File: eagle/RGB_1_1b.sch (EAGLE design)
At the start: 16 parts, among them X1 RGB, X2 Buzzer

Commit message: Missing doc files added, schematics.pdf created +doc/pdf/schematics.pdf: all schematics in one file
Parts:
- R2: value 4k7 -> 680
- R3: value 10k -> 4k7
- R4: value 2k2 -> 470
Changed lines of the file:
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@@
 <?xml version="1.0" encoding="utf-8"?>
 <!DOCTYPE eagle SYSTEM "eagle.dtd">
-<eagle version="7.6.0">
+<eagle version="8.3.2">
 <drawing>
 <settings>
 <setting alwaysvectorfont="no"/>
+<setting keepoldvectorfont="yes"/>
 <setting verticaltext="up"/>
 </settings>
@@
 <part name="P1" library="01-my-led" deviceset="RGB-5MM" device=""/>
 <part name="R1" library="01-my_rcl" deviceset="R-EU_" device="0207/10" value="220"/>
-<part name="R2" library="01-my_rcl" deviceset="R-EU_" device="0207/10" value="4k7"/>
-<part name="R3" library="01-my_rcl" deviceset="R-EU_" device="0207/10" value="10k"/>
-<part name="R4" library="01-my_rcl" deviceset="R-EU_" device="0207/10" value="2k2"/>
+<part name="R2" library="01-my_rcl" deviceset="R-EU_" device="0207/10" value="680"/>
+<part name="R3" library="01-my_rcl" deviceset="R-EU_" device="0207/10" value="4k7"/>
+<part name="R4" library="01-my_rcl" deviceset="R-EU_" device="0207/10" value="470"/>
 <part name="GND5" library="supply1" deviceset="GND" device=""/>
 <part name="P2" library="01-my-led" deviceset="LED" device="5MM"/>

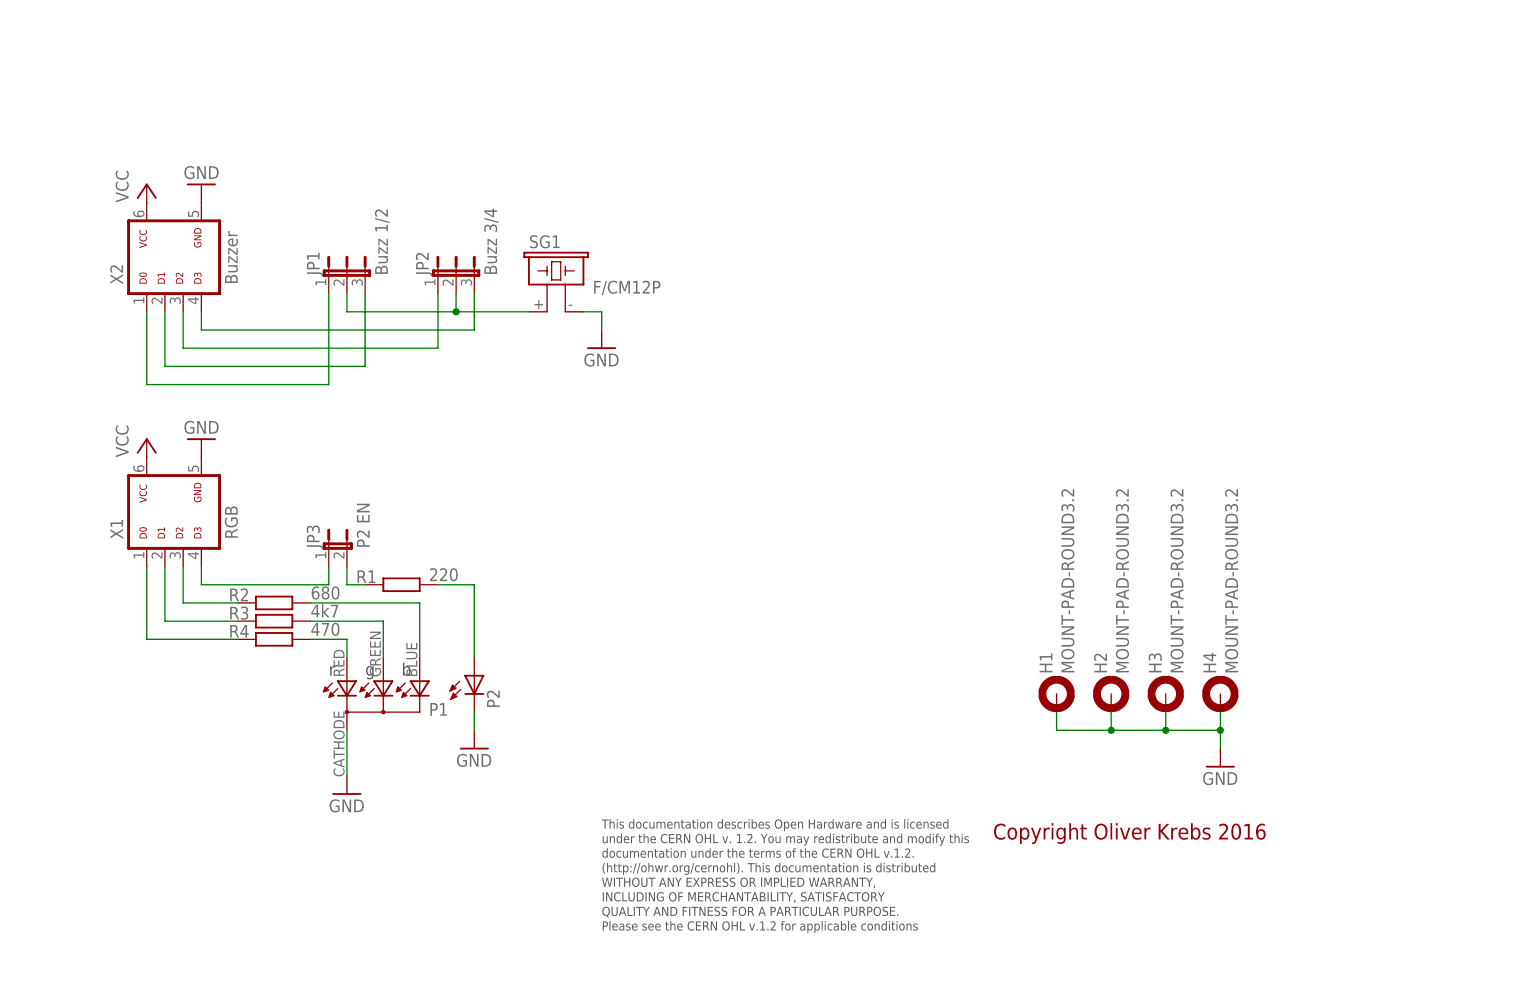
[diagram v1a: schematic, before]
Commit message: Add new tetra-Board and arduino files
Add AMP_1_0, AVC_1_0, D18_1_1, IOP_1_2, MIC_1_0, PIN_1_1, POT_1_0, PWA_1_0, PWR_1_0, RGF 2.0, SOC_2_0, VLT_1_0
Add mex_nano_shield_keyboard, mex_nano_shied_numbers

New arduino projects
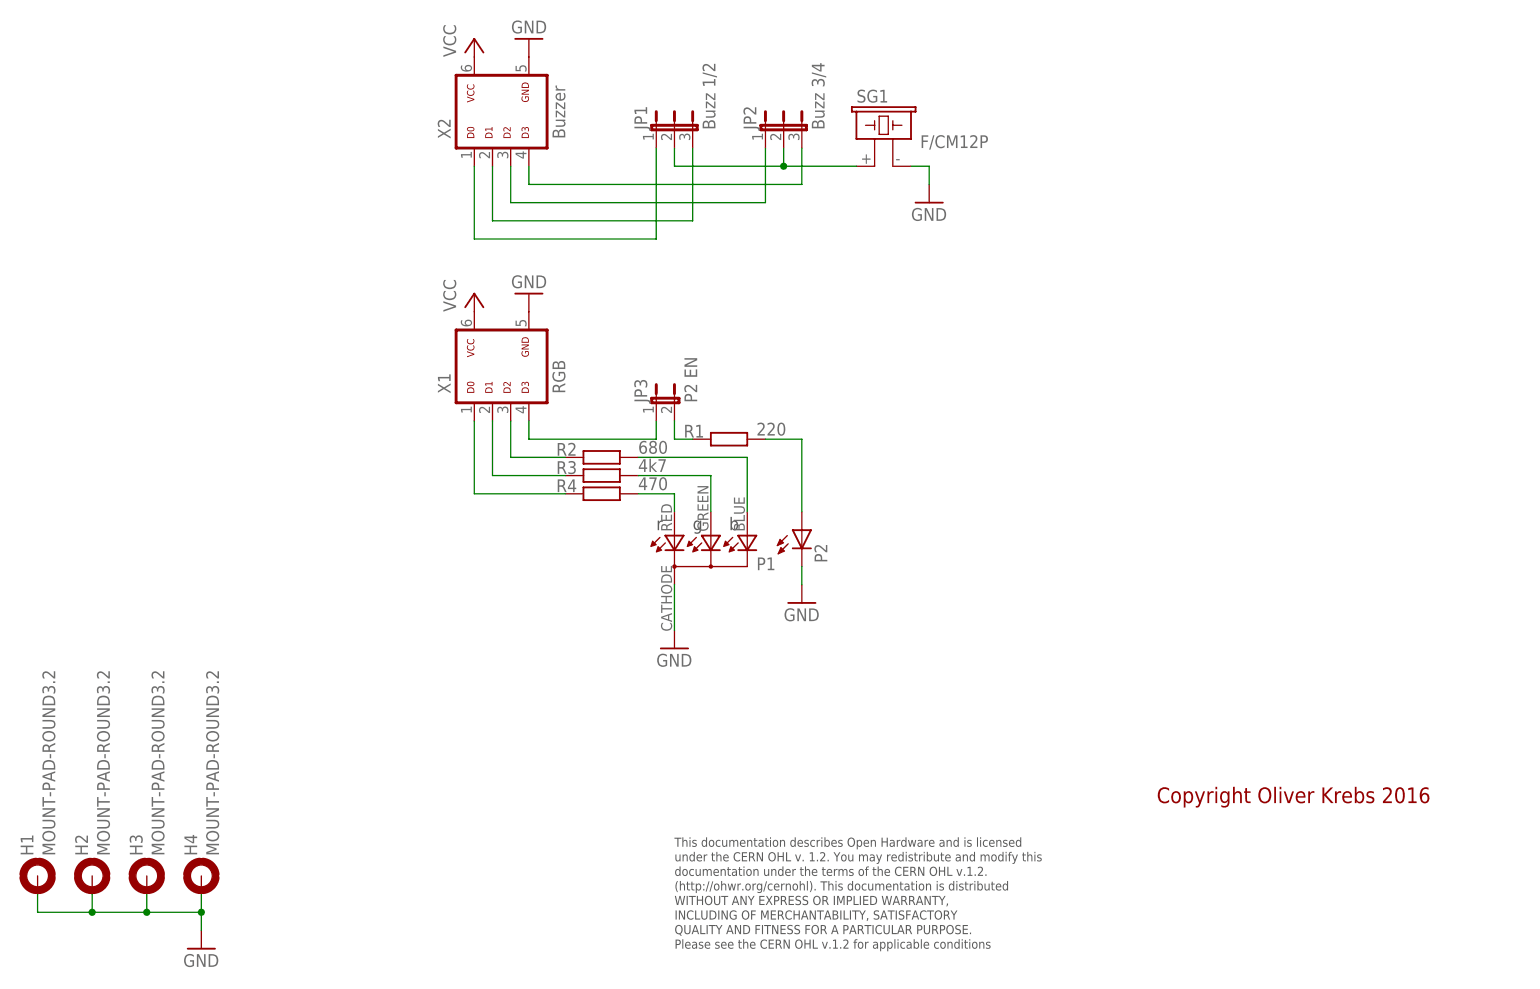
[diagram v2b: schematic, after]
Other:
- moved on the sheet: H1, H2, H3, H4, JP1, JP2, JP3, P1, P2, R1, R2, R3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
